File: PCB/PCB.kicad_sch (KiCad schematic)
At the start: 59 parts, among them J1 USB_C_Receptacle_USB2.0_16P, Q2 IRLML2060, SW1 SW_Push, SW2 SW_Push, U1 RP2040, U2 USBLC6-2SC6, U3 NCP1117ST33T3G, U4 W25Q32JVSS, U5 Conn, U6 ST25DV04K-JFR6D3, Y1 Crystal_GND24

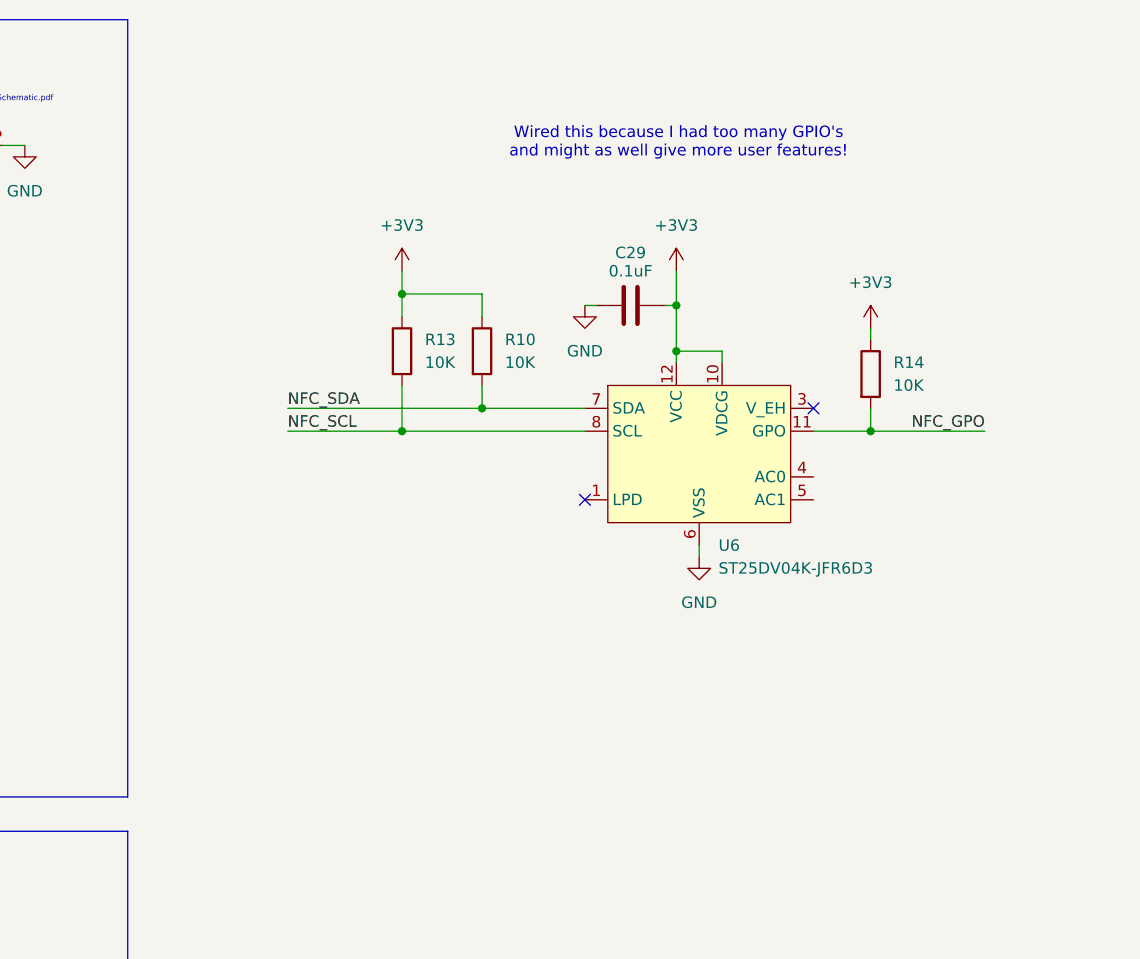
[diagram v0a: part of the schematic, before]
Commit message: finished the NFC antenna
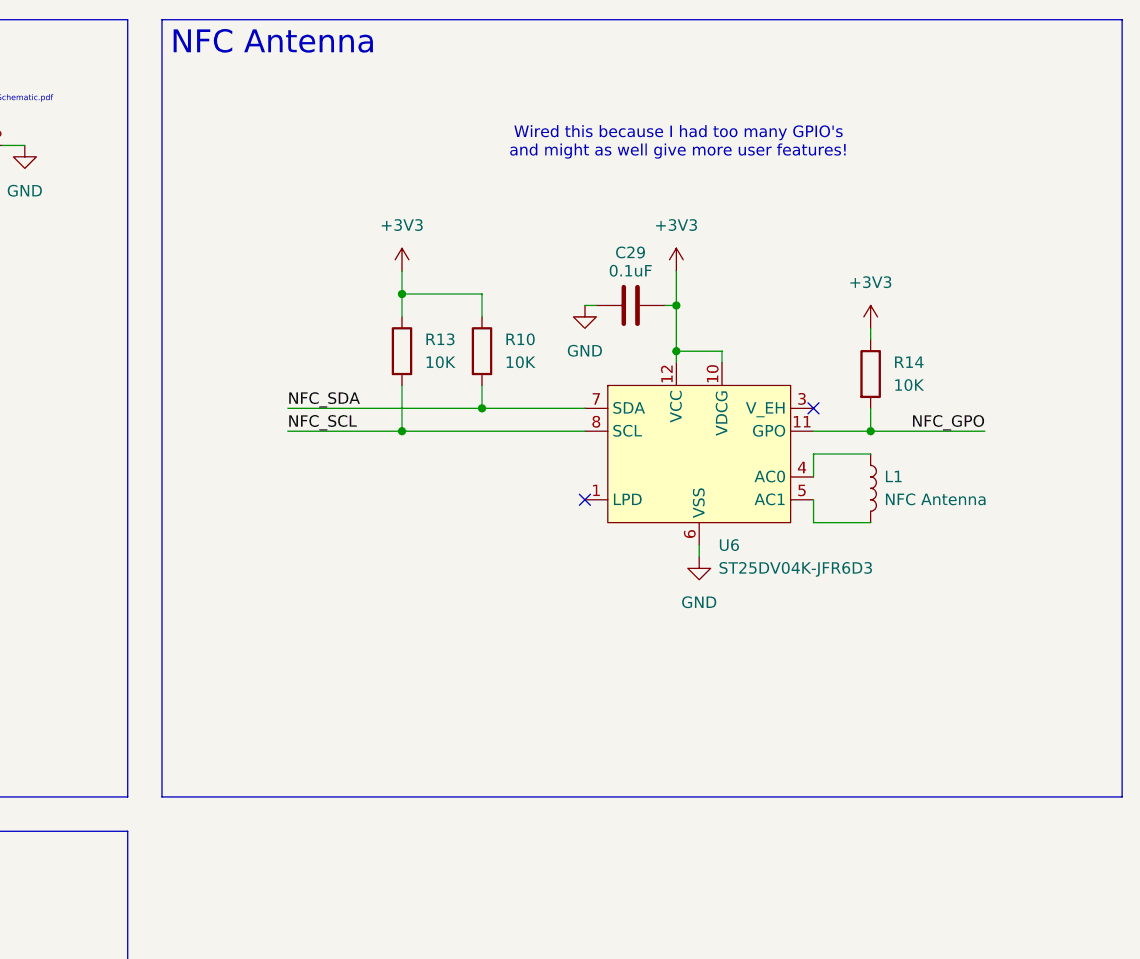
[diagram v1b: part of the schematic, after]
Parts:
- added L1: NFC Antenna, symbol Device:L
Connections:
- net at U6.4 (AC0): now also L1.1
- net at U6.5 (AC1): now also L1.2
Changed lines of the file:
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@@
 		)
 	)
+	(text_box "NFC Antenna"
+		(exclude_from_sim no)
+		(at 297.18 15.24 0)
+		(size 106.68 86.36)
+		(margins 0.9525 0.9525 0.9525 0.9525)
+		(stroke
+			(width 0)
+			(type solid)
+		)
+		(fill
+			(type none)
+		)
+		(effects
+			(font
+				(size 2.54 2.54)
+			)
+			(justify left top)
+		)
+	)
 	(junction
 		(at 181.61 142.24)
@@
 	(wire
 		(pts
+			(xy 369.57 68.58) (xy 369.57 71.12)
+		)
+		(stroke
+			(width 0)
+			(type default)
+		)
+	)
+	(wire
+		(pts
 			(xy 233.68 85.09) (xy 233.68 82.55)
 		)
@@
 	(wire
 		(pts
+			(xy 369.57 71.12) (xy 375.92 71.12)
+		)
+		(stroke
+			(width 0)
+			(type default)
+		)
+	)
+	(wire
+		(pts
 			(xy 119.38 132.08) (xy 119.38 130.81)
 		)
@@
 	(wire
 		(pts
+			(xy 369.57 63.5) (xy 375.92 63.5)
+		)
+		(stroke
+			(width 0)
+			(type default)
+		)
+	)
+	(wire
+		(pts
 			(xy 62.23 175.26) (xy 74.93 175.26)
 		)
@@
 	(wire
 		(pts
+			(xy 369.57 66.04) (xy 369.57 63.5)
+		)
+		(stroke
+			(width 0)
+			(type default)
+		)
+	)
+	(wire
+		(pts
 			(xy 62.23 173.99) (xy 62.23 175.26)
 		)
@@
 					(unit 1)
 				)
+			)
+		)
+	)
+	(symbol
+		(lib_id "Device:L")
+		(at 375.92 67.31 0)
+		(unit 1)
+		(exclude_from_sim no)
+		(in_bom yes)
+		(on_board yes)
+		(dnp no)
+		(property "Reference" "L1"
+			(at 377.444 66.04 0)
+			(effects
+				(font
+					(size 1.27 1.27)
+				)
+				(justify left)
+			)
+		)
+		(property "Value" "NFC Antenna"
+			(at 377.444 68.58 0)
+			(effects
+				(font
+					(size 1.27 1.27)
+				)
+				(justify left)
+			)
+		)
+		(property "Footprint" ""
+			(at 375.92 67.31 0)
+			(effects
+				(font
+					(size 1.27 1.27)
+				)
+				(hide yes)
+			)
+		)
+		(property "Datasheet" "~"
+			(at 375.92 67.31 0)
+			(effects
+				(font
+					(size 1.27 1.27)
+				)
+				(hide yes)
+			)
+		)
+		(property "Description" "Inductor"
+			(at 375.92 67.31 0)
+			(effects
+				(font
+					(size 1.27 1.27)
+				)
+				(hide yes)
+			)
+		)
+		(pin "1"
+		)
+		(pin "2"
+		)
+		(instances
+			(project ""
+				(path "/f82e74e4-6971-48c6-8666-d0a9e9f61139"
+					(reference "L1")
+					(unit 1)
+				)

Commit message: assigning all passive footprints
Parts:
- C1, C2: footprint (none) -> Capacitor_SMD:C_0805_2012Metric
- C10, C11, C12, C13, C14, C15, C16, C17, C18, C19, C20, C21, C22, C23, C24, C25, C26, C29, C3, C4, C5, C6, C7, C8, C9: footprint (none) -> Capacitor_SMD:C_0402_1005Metric
- C27, C28: footprint (none) -> Capacitor_SMD:C_0603_1608Metric
- D1: footprint (none) -> LED_SMD:LED_0805_2012Metric
- R1, R10, R11, R12, R13, R14, R2, R3, R4, R5, R6, R7, R8, R9: footprint (none) -> Resistor_SMD:R_0402_1005Metric
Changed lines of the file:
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@@
 			)
 		)
-		(property "Footprint" ""
+		(property "Footprint" "Resistor_SMD:R_0402_1005Metric"
 			(at 60.452 170.18 90)
 			(effects
@@
 			)
 		)
-		(property "Footprint" ""
+		(property "Footprint" "Resistor_SMD:R_0402_1005Metric"
 			(at 322.072 52.07 90)
 			(effects
@@
 			)
 		)
-		(property "Footprint" ""
+		(property "Footprint" "Capacitor_SMD:C_0402_1005Metric"
 			(at 197.8152 140.97 0)
 			(effects
@@
 			)
 		)
-		(property "Footprint" ""
+		(property "Footprint" "Resistor_SMD:R_0402_1005Metric"
 			(at 73.66 218.948 90)
 			(effects
@@
 			)
 		)
-		(property "Footprint" ""
+		(property "Footprint" "Capacitor_SMD:C_0402_1005Metric"
 			(at 159.7152 140.97 0)
 			(effects
@@
 			)
 		)
-		(property "Footprint" ""
+		(property "Footprint" "Capacitor_SMD:C_0402_1005Metric"
 			(at 238.76 69.85 0)
 			(effects
@@
 			)
 		)
-		(property "Footprint" ""
+		(property "Footprint" "Resistor_SMD:R_0402_1005Metric"
 			(at 176.022 81.28 90)
 			(effects
@@
 			)
 		)
-		(property "Footprint" ""
+		(property "Footprint" "Capacitor_SMD:C_0603_1608Metric"
 			(at 170.4848 55.88 0)
 			(effects
@@
 			)
 		)
-		(property "Footprint" ""
+		(property "Footprint" "Capacitor_SMD:C_0805_2012Metric"
 			(at 107.6452 49.53 0)
 			(effects
@@
 			)
 		)
-		(property "Footprint" ""
+		(property "Footprint" "Capacitor_SMD:C_0402_1005Metric"
 			(at 127.9652 140.97 0)
 			(effects
@@
 			)
 		)
-		(property "Footprint" ""
+		(property "Footprint" "Capacitor_SMD:C_0402_1005Metric"
 			(at 264.16 195.8848 0)
 			(effects
@@
 			)
 		)
-		(property "Footprint" ""
+		(property "Footprint" "Capacitor_SMD:C_0402_1005Metric"
 			(at 238.76 34.29 0)
 			(effects
@@
 			)
 		)
-		(property "Footprint" ""
+		(property "Footprint" "Capacitor_SMD:C_0805_2012Metric"
 			(at 79.7052 49.53 0)
 			(effects
@@
 			)
 		)
-		(property "Footprint" ""
+		(property "Footprint" "Capacitor_SMD:C_0402_1005Metric"
 			(at 112.7252 140.97 0)
 			(effects
@@
 			)
 		)
-		(property "Footprint" ""
+		(property "Footprint" "Capacitor_SMD:C_0402_1005Metric"
 			(at 190.1952 140.97 0)
 			(effects
@@
 			)
 		)
-		(property "Footprint" ""
+		(property "Footprint" "Resistor_SMD:R_0402_1005Metric"
 			(at 187.452 81.28 90)
 			(effects
@@
 			)
 		)
-		(property "Footprint" ""
+		(property "Footprint" "Resistor_SMD:R_0402_1005Metric"
 			(at 330.962 52.07 90)
 			(effects
@@
 			)
 		)
-		(property "Footprint" ""
+		(property "Footprint" "Resistor_SMD:R_0402_1005Metric"
 			(at 220.98 211.328 90)
 			(effects
@@
 			)
 		)
-		(property "Footprint" ""
+		(property "Footprint" "Capacitor_SMD:C_0402_1005Metric"
 			(at 152.0952 140.97 0)
 			(effects
@@
 			)
 		)
-		(property "Footprint" ""
+		(property "Footprint" "Capacitor_SMD:C_0402_1005Metric"
 			(at 120.3452 140.97 0)
 			(effects
@@
 			)
 		)
-		(property "Footprint" ""
+		(property "Footprint" "Resistor_SMD:R_0402_1005Metric"
 			(at 57.15 50.038 90)
 			(effects
@@
 			)
 		)
-		(property "Footprint" ""
+		(property "Footprint" "Capacitor_SMD:C_0402_1005Metric"
 			(at 144.4752 140.97 0)
 			(effects
@@
 			)
 		)
-		(property "Footprint" ""
+		(property "Footprint" "Resistor_SMD:R_0402_1005Metric"
 			(at 120.65 184.658 90)
 			(effects
@@
 			)
 		)
-		(property "Footprint" ""
+		(property "Footprint" "Capacitor_SMD:C_0402_1005Metric"
 			(at 44.45 206.0448 0)
 			(effects
@@
 			)
 		)
-		(property "Footprint" ""
+		(property "Footprint" "Capacitor_SMD:C_0402_1005Metric"
 			(at 243.84 36.83 0)
 			(effects
@@
 			)
 		)
-		(property "Footprint" ""
+		(property "Footprint" "Capacitor_SMD:C_0603_1608Metric"
 			(at 190.1952 52.07 0)
 			(effects
@@
 			)
 		)
-		(property "Footprint" ""
+		(property "Footprint" "Resistor_SMD:R_0402_1005Metric"
 			(at 57.15 47.498 90)
 			(effects
@@
 			)
 		)
-		(property "Footprint" ""
+		(property "Footprint" "Capacitor_SMD:C_0402_1005Metric"
 			(at 44.45 216.2048 0)
 			(effects
@@
 			)
 		)
-		(property "Footprint" ""
+		(property "Footprint" "Capacitor_SMD:C_0402_1005Metric"
 			(at 238.76 85.09 0)
 			(effects
@@
 			)
 		)
-		(property "Footprint" ""
+		(property "Footprint" "Capacitor_SMD:C_0402_1005Metric"
 			(at 243.84 72.39 0)
 			(effects
@@
 			)
 		)
-		(property "Footprint" ""
+		(property "Footprint" "Capacitor_SMD:C_0402_1005Metric"
 			(at 238.76 62.23 0)
 			(effects
@@
 			)
 		)
-		(property "Footprint" ""
+		(property "Footprint" "LED_SMD:LED_0805_2012Metric"
 			(at 62.23 142.24 0)
 			(effects
@@
 			)
 		)
-		(property "Footprint" ""
+		(property "Footprint" "Resistor_SMD:R_0402_1005Metric"
 			(at 53.34 144.018 90)
 			(effects
@@
 			)
 		)
-		(property "Footprint" ""
+		(property "Footprint" "Resistor_SMD:R_0402_1005Metric"
 			(at 120.65 187.198 90)
 			(effects
@@
 			)
 		)
-		(property "Footprint" ""
+		(property "Footprint" "Capacitor_SMD:C_0402_1005Metric"
 			(at 167.3352 140.97 0)
 			(effects
@@
 			)
 		)
-		(property "Footprint" ""
+		(property "Footprint" "Capacitor_SMD:C_0402_1005Metric"
 			(at 238.76 80.01 0)
 			(effects
@@
 			)
 		)
-		(property "Footprint" ""
+		(property "Footprint" "Capacitor_SMD:C_0402_1005Metric"
 			(at 182.5752 140.97 0)
 			(effects
@@
 			)
 		)
-		(property "Footprint" ""
+		(property "Footprint" "Capacitor_SMD:C_0402_1005Metric"
 			(at 238.76 74.93 0)
 			(effects
@@
 			)
 		)
-		(property "Footprint" ""
+		(property "Footprint" "Resistor_SMD:R_0402_1005Metric"
 			(at 228.092 203.2 90)
 			(effects
@@
 			)
 		)
-		(property "Footprint" ""
+		(property "Footprint" "Capacitor_SMD:C_0402_1005Metric"
 			(at 243.84 82.55 0)
 			(effects
@@
 			)
 		)
-		(property "Footprint" ""
+		(property "Footprint" "Capacitor_SMD:C_0402_1005Metric"
 			(at 174.9552 140.97 0)
 			(effects
@@
 			)
 		)
-		(property "Footprint" ""
+		(property "Footprint" "Capacitor_SMD:C_0402_1005Metric"
 			(at 243.84 77.47 0)
 			(effects
@@
 			)
 		)
-		(property "Footprint" ""
+		(property "Footprint" "Resistor_SMD:R_0402_1005Metric"
 			(at 374.142 54.61 90)
 			(effects
@@
 			)
 		)
-		(property "Footprint" ""
+		(property "Footprint" "Capacitor_SMD:C_0402_1005Metric"
 			(at 353.06 46.0248 0)
 			(effects
